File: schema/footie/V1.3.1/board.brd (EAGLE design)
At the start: 44.2 x 46.7 mm, 44 parts, among them T1 2N3565, U1 IRLML2246TRPBF, U2 USD-SOCKETNEW, U3 HC_05, U4 MCP73831, U5 3.3 regulator, U6 ATMEGA328P-AU

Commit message: finished route pcb expect antenna
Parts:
- moved C2 13.4 mm to (16.6, 41.2), turned to 0 degrees
- moved C3 7.18 mm to (30.1, 42.9), turned to 90 degrees
- moved C9 5.52 mm to (28.1, 38.9)
- moved U1 2.52 mm to (21.6, 39.2), turned to 270 degrees
- moved R9 2.11 mm to (5.48, 44.5)
- moved JP2 1.71 mm to (5.73, 36.3)
- moved U5 1.30 mm to (21.7, 43.6)
- moved C8 1.30 mm to (16.4, 43.9)
- moved U4 1.30 mm to (11.4, 42.6)
- moved C4 1.10 mm to (26.0, 43.6)
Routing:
- net +3V3: track 37.1 -> 160.4 mm, vias 1 -> 12
- net ARDUINO_TX: track 0.00 -> 81.3 mm, vias 0 -> 9
- net ARDUINO_RX: track 0.00 -> 71.4 mm, vias 0 -> 7
- net N$2: track 0.00 -> 65.1 mm, vias 0 -> 5
- net SD_MOSI: track 0.00 -> 64.7 mm, vias 0 -> 8
- net D3: track 0.00 -> 44.3 mm, vias 0 -> 2
- net D5: track 0.00 -> 43.3 mm, vias 0 -> 2
- net N$11: track 0.00 -> 43.2 mm, vias 0 -> 2
- net D2: track 0.00 -> 41.5 mm, vias 0 -> 2
- net DTR: track 0.00 -> 38.7 mm, vias 0 -> 3
- net N$20: track 0.00 -> 37.9 mm, vias 0 -> 6
- net SD_SCK: track 0.00 -> 37.3 mm, vias 0 -> 4
- net SD_MISO: track 0.00 -> 31.0 mm, vias 0 -> 1
- net GPSTX: track 0.00 -> 30.4 mm, vias 0 -> 2
- net VCC: track 0.00 -> 28.1 mm, vias 0 -> 2
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- added copper zone on layer 1, net GND
- added copper zone on layer 16, net GND
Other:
- board size 44.2 x 46.7 mm -> 46.1 x 49.1 mm

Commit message: finished route pcb expect antenna
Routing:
- net N$2: track 65.1 -> 64.0 mm
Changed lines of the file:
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@@
 <wire x1="19.2" y1="31.7" x2="21.3" y2="31.7" width="0.254" layer="16"/>
 <wire x1="18.7" y1="31.3" x2="19.2" y2="31.7" width="0.254" layer="16"/>
-<wire x1="18.7" y1="32.7" x2="18.7" y2="31.3" width="0.254" layer="1"/>
-<wire x1="11.3" y1="37" x2="18.7" y2="32.7" width="0.254" layer="1"/>
+<wire x1="17.9" y1="32.6" x2="18.7" y2="31.3" width="0.254" layer="1"/>
+<wire x1="11.3" y1="37" x2="15.5" y2="32.7" width="0.254" layer="1"/>
+<wire x1="15.5" y1="32.7" x2="16.4" y2="32.7" width="0.254" layer="1"/>
+<wire x1="16.4" y1="32.7" x2="17.9" y2="32.6" width="0.254" layer="1"/>
 <via x="13.8" y="17.8" extent="1-16" drill="0.6"/>
 <via x="20.6" y="18.1" extent="1-16" drill="0.6"/>
@@
 <wire x1="30" y1="29.6" x2="30" y2="28.5" width="0.254" layer="1"/>
 <wire x1="27.6" y1="32" x2="30" y2="29.6" width="0.254" layer="1"/>
-<wire x1="27.6" y1="34" x2="27.6" y2="32" width="0.254" layer="1"/>
-<wire x1="27.1" y1="34.5" x2="27.6" y2="34" width="0.254" layer="1"/>
-<wire x1="25.3" y1="34.5" x2="27.1" y2="34.5" width="0.254" layer="1"/>
+<wire x1="26.8" y1="33" x2="27.6" y2="32" width="0.254" layer="1"/>
+<wire x1="25.3" y1="34.5" x2="26.8" y2="33" width="0.254" layer="1"/>
 <wire x1="22.8" y1="37.2" x2="25.3" y2="34.5" width="0.254" layer="1"/>
 <wire x1="22.4" y1="36.8" x2="22.8" y2="37.2" width="0.254" layer="16"/>
@@
 <wire x1="32.5" y1="24.4" x2="32.5" y2="15.9" width="0.254" layer="16"/>
 <wire x1="28.7" y1="28.2" x2="32.5" y2="24.4" width="0.254" layer="16"/>
-<wire x1="22.8" y1="34.1" x2="28.7" y2="28.2" width="0.254" layer="1"/>
-<wire x1="22.8" y1="34.3" x2="22.8" y2="34.1" width="0.254" layer="1"/>
+<wire x1="28.4" y1="28.6" x2="28.7" y2="28.2" width="0.254" layer="1"/>
+<wire x1="22.8" y1="34.3" x2="28.4" y2="28.6" width="0.254" layer="1"/>
 <wire x1="18.4" y1="38.7" x2="22.8" y2="34.3" width="0.254" layer="1"/>
 <wire x1="15.7" y1="38.7" x2="18.4" y2="38.7" width="0.254" layer="1"/>

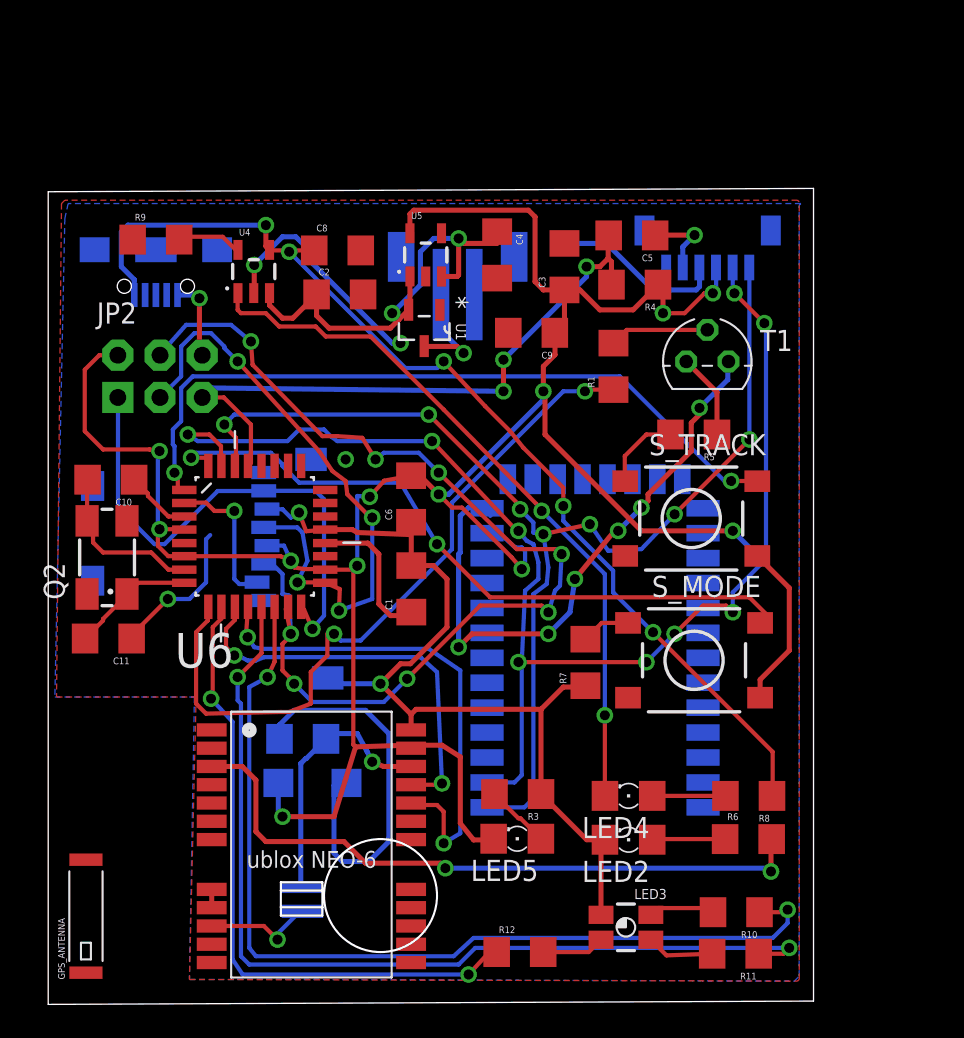
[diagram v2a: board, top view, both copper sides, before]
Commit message: complete the board layout
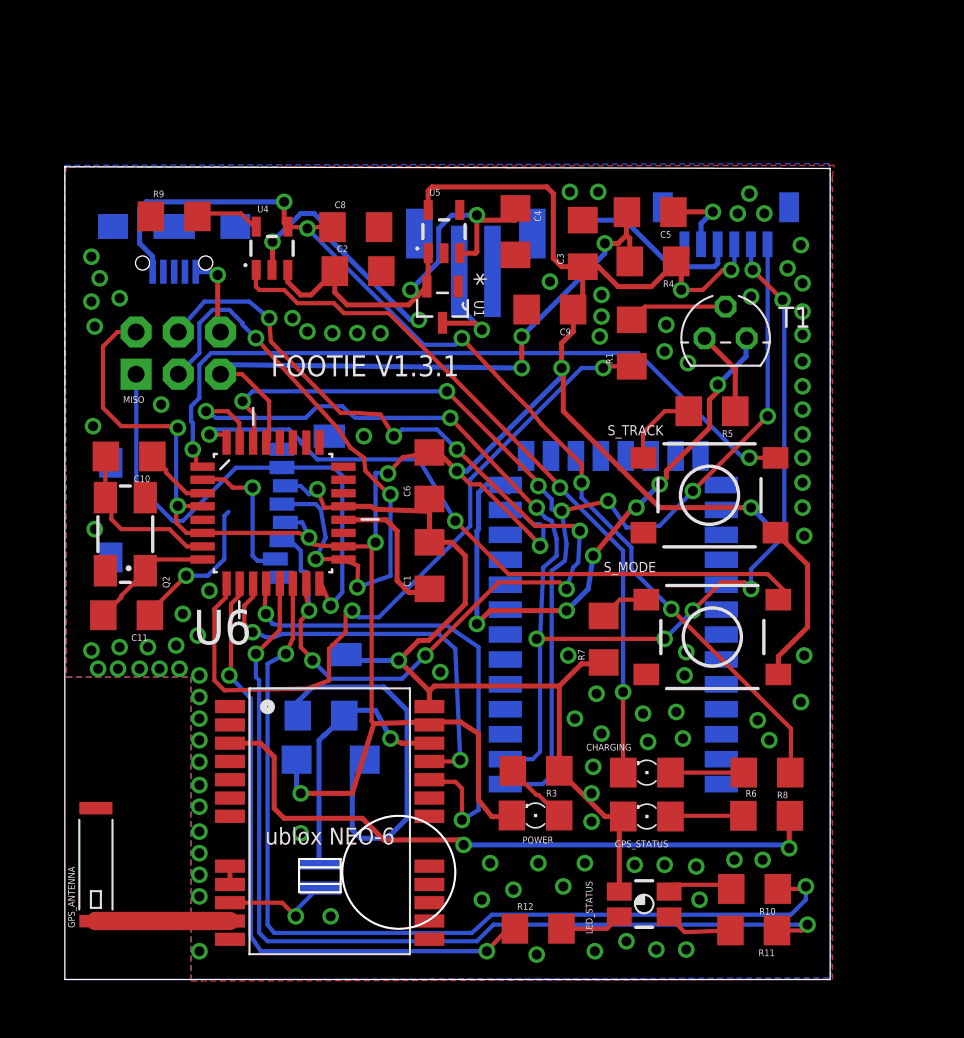
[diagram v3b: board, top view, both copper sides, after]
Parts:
- removed LED2, LED4, LED5: (no value), eagle-ltspice:LED_1206
- removed LED3: LED_RGB_PLCC_AVAGO_MTB0, pretender:LED_RGB_PLCC_AVAGO_MTB0
- removed U$2: JST_VERTICAL, SparkFun-Connectors:JST-6-SMD-VERT-1.0MM
- removed U3: HC_05, SerialPortBluetooth:BLUETOOTH_SMD
- added BLUETOOTH: HC_05, SerialPortBluetooth:BLUETOOTH_SMD
- added CHARGING, GPS_STATUS: (no value), eagle-ltspice:LED_1206
- added DEBUG: JST_VERTICAL, SparkFun-Connectors:JST-6-SMD-VERT-1.0MM
- added LED_STATUS: LED_RGB_PLCC_AVAGO_MTB0, pretender:LED_RGB_PLCC_AVAGO_MTB0
- added POWER: red, eagle-ltspice:LED_1206
- moved GPS_ANTENNA 3.16 mm to (1.87, 6.91)
- moved R5 1.78 mm to (39.0, 34.2)
- moved T1 1.78 mm to (39.8, 38.6)
- moved JP2 1.78 mm to (6.83, 37.7)
- moved C2 1.78 mm to (17.6, 42.6)
- moved R7 1.78 mm to (32.4, 20.5)
- moved C10 1.78 mm to (3.87, 31.5)
- moved C11 1.78 mm to (3.72, 21.9)
- moved Q2 1.78 mm to (3.64, 26.8)
- moved R10 1.78 mm to (41.5, 5.45)
- moved R6 1.78 mm to (42.2, 9.85)
- moved R11 1.78 mm to (41.5, 2.95)
- moved D1 1.78 mm to (16.0, 13.2)
- moved R2 1.78 mm to (15.4, 15.9)
- moved U$3 1.78 mm to (14.1, 7.25)
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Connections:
- net +3V3: now also BLUETOOTH.12, DEBUG.4, POWER.C; no longer LED5.C, U$2.4, U3.12
- net ARDUINO_RX: now also BLUETOOTH.1, DEBUG.6; no longer U$2.6, U3.1
- net ARDUINO_TX: now also BLUETOOTH.2, DEBUG.5; no longer U$2.5, U3.2
- net GND: now also BLUETOOTH.21, BLUETOOTH.22, DEBUG.3, GPS_STATUS.C, LED_STATUS.1; no longer LED2.C, LED3.1, U$2.3, U3.21, U3.22
- net N$11: now also CHARGING.C; no longer LED4.C
- net N$13: now also DEBUG.2; no longer U$2.2
- net N$16: now also POWER.A; no longer LED5.A
- net N$17: now also LED_STATUS.3; no longer LED3.3
- net N$18: now also LED_STATUS.4; no longer LED3.4
- net N$20: now also BLUETOOTH.13; no longer U3.13
- net N$21: now also LED_STATUS.2; no longer LED3.2
- net N$4: now also GPS_STATUS.A; no longer LED2.A
- net N$8: now also CHARGING.A; no longer LED4.A
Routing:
- net N$7: track 0.00 -> 8.08 mm
- net GND: vias 8 -> 108
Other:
- board size 46.1 x 49.1 mm -> 46.1 x 48.9 mm
- board text added: "FOOTIE V1.3.1"
- board text added: "MISO"

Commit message: complete board but not happy
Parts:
- removed GPS_ANTENNA: ANTENNA2SMD6, SparkFun-RF:ANTENNA-CHIP6
- removed U$1: UBLOX_NEO-6, Ava:UBLOX_NEO-6P
- added C7: 4.7 uF, SparkFun-Capacitors:1206
- added R13, R14: 220 Ohm, SparkFun-Passives:1206
- added U3: CAM-M8Q, CAM-M8Q:CAM-M8Q
- moved BLUETOOTH 38.1 mm to (40.7, 47.1), turned to 0 degrees
- moved R5 32.7 mm to (24.1, 5.08), flipped to the bottom, turned to 0 degrees
- moved S_TRACK 28.2 mm to (24.1, 5.08)
- moved BATTERY_CONNECTOR 21.9 mm to (4.28, 52.5), flipped to the top
- moved C3 20.7 mm to (10.5, 43.7), turned to 0 degrees
- moved R6 19.5 mm to (23.5, 15.1), turned to 180 degrees
- moved R8 18.8 mm to (23.5, 12.5), turned to 0 degrees
- moved C4 18.4 mm to (10.6, 53.2)
- moved R9 17.2 mm to (23.8, 46.0), turned to 90 degrees
- moved T1 16.4 mm to (37.5, 22.3)
- moved U2 16.3 mm to (16.3, 41.6), turned to 270 degrees
- moved U1 16.1 mm to (8.19, 47.4), turned to 90 degrees
- moved R7 16.0 mm to (36.8, 5.08), flipped to the bottom, turned to 0 degrees
- moved S_MODE 15.7 mm to (36.8, 5.08)
- moved R1 15.6 mm to (32.6, 22.8)
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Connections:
- removed net N$6 (its old number): R2.1, U$1.22_V_BCKP, U$3.3V
- removed net N$7: GPS_ANTENNA.1, U$1.11_RF_IN
- removed net SCL: U$1.19_SCL2
- removed net SDA: U$1.18_SDA2
- new net N$25: R13.1, U3.25
- new net N$26: R14.1, U3.26
- new net N$4: R6.2, U3.29
- net +3V3: now also C7.1, U3.1, U3.9; no longer U$1.23_VCC
- net GND: now also C7.2, U3.10, U3.11, U3.12, U3.13, U3.14, U3.15, U3.18, U3.19, U3.21, U3.22, U3.27, U3.31, U3.4, U3.5; no longer U$1.10_GND, U$1.12_GND, U$1.13_GND, U$1.24_GND, U$1.7_VDDUSB
- net GPSRX: now also R14.2; no longer U$1.21_RXD1
- net GPSTX: now also R13.2; no longer U$1.20_TXD1
- net N$3: now also U3.16, U3.17; no longer R6.2, U$1.3_TIMEPULSE
- net N$5: now also R2.1, U$3.3V, U3.8; no longer U$1.8_RESERVED, U$1.9_VCC_RF
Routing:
- net GND: track 111.9 -> 280.7 mm, vias 108 -> 71
- net +3V3: track 160.4 -> 245.0 mm, vias 12 -> 16
- net N$3: track 40.1 -> 1.00 mm, vias 2 -> 0
- net ARDUINO_TX: track 81.3 -> 43.3 mm, vias 9 -> 3
- net D10: track 57.3 -> 22.0 mm
- net N$5: track 1.10 -> 35.1 mm, vias 0 -> 2
- net N$20: track 37.9 -> 7.60 mm, vias 6 -> 0
- net D9: track 57.3 -> 27.7 mm, vias 2 -> 0
- net ARDUINO_RX: track 71.4 -> 44.3 mm, vias 7 -> 4
- net GPSTX: track 30.4 -> 7.66 mm, vias 2 -> 0
- net N$1: track 23.8 -> 2.10 mm
- net N$2: track 64.0 -> 84.9 mm, vias 5 -> 6
- net DTR: track 38.7 -> 58.4 mm, vias 3 -> 7
- net SD_CS: track 8.87 -> 26.8 mm
- net D5: track 43.3 -> 25.5 mm, vias 2 -> 4
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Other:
- board size 46.1 x 48.9 mm -> 42.9 x 57 mm
- board text removed: "FOOTIE V1.3.1"
- board text removed: "MISO"

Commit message: update version, bit bigger but better design
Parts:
- moved BATTERY_CONNECTOR 48.5 mm to (48.4, 32.1), turned to 270 degrees
- moved U1 39.5 mm to (42.7, 28.3), turned to 270 degrees
- moved C4 33.9 mm to (39.7, 35.8), turned to 180 degrees
- moved C3 32.0 mm to (38.3, 27.9), turned to 270 degrees
- moved U5 31.2 mm to (39.8, 32.2)
- moved C9 26.2 mm to (35.5, 27.8)
- moved C5 20.7 mm to (43.7, 42.3), turned to 270 degrees
- moved R11 15.2 mm to (48.5, 6.81), turned to 180 degrees
- moved R10 15.0 mm to (43.8, 3.90), turned to 270 degrees
- moved R1 14.3 mm to (43.2, 13.2)
- moved R12 14.1 mm to (48.5, 9.58)
- moved LED_STATUS 12.5 mm to (48.5, 2.84), turned to 270 degrees
- moved JP2 12.2 mm to (19.9, 41.5), turned to 90 degrees
- moved C8 12.1 mm to (32.1, 40.3), turned to 270 degrees
- moved BLUETOOTH 11.2 mm to (48.9, 39.5)
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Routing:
- net GND: track 280.7 -> 203.3 mm, vias 71 -> 56
- net +3V3: track 245.0 -> 187.5 mm, vias 16 -> 14
- net N$2: track 84.9 -> 39.1 mm, vias 6 -> 2
- net SD_MOSI: track 71.7 -> 35.7 mm, vias 7 -> 6
- net N$11: track 52.2 -> 29.2 mm, vias 4 -> 2
- net ARDUINO_TX: track 43.3 -> 62.0 mm
- net D9: track 27.7 -> 45.8 mm, vias 0 -> 2
- net DTR: track 58.4 -> 41.2 mm, vias 7 -> 3
- net D10: track 22.0 -> 37.0 mm
- net D6: track 34.0 -> 48.8 mm
- net D5: track 25.5 -> 39.1 mm, vias 4 -> 2
- net SD_MISO: track 29.8 -> 42.0 mm, vias 2 -> 4
- net SD_CS: track 26.8 -> 16.6 mm
- net N$13: track 10.5 -> 2.30 mm, vias 2 -> 0
- net ARDUINO_RX: track 44.3 -> 51.3 mm, vias 4 -> 5
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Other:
- board size 42.9 x 57 mm -> 53 x 50.6 mm

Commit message: update final version + library
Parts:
- S_MODE: value DTSM-6 -> MODE
- S_TRACK: value DTSM-6 -> TRACK
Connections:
- net GND: no longer BLUETOOTH.21, BLUETOOTH.22
- net N$20: now also BLUETOOTH.21, BLUETOOTH.22
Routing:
- net N$20: track 13.8 -> 28.7 mm
- net ARDUINO_TX: track 62.0 -> 63.1 mm
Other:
- board text added: "FOOTIE V1.3.1"

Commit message: update stuff2
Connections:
- net +3V3: now also LED_STATUS.1
- net GND: no longer LED_STATUS.1
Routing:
- net GND: track 203.3 -> 188.5 mm, vias 56 -> 54
- net +3V3: track 187.5 -> 198.0 mm, vias 14 -> 16
- net N$2: track 39.1 -> 41.8 mm
- net DTR: track 41.2 -> 43.0 mm
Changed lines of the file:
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@@
 </element>
 <element name="C7" library="SparkFun-Capacitors" package="1206" value="4.7 uF" x="3.2" y="17.04">
-<attribute name="OC_FARNELL" value="2497081" x="3.2" y="17.04" size="1.778" layer="27" display="off"/>
+<attribute name="OC_FARNELL" value="2497114" x="3.2" y="17.04" size="1.778" layer="27" display="off"/>
 <attribute name="MF" value="WALSIN" x="3.2" y="17.04" size="1.778" layer="27" display="off"/>
-<attribute name="MPN" value="1206B106K160CT" x="3.2" y="17.04" size="1.778" layer="27" display="off"/>
+<attribute name="MPN" value="1206B475K500CT" x="3.2" y="17.04" size="1.778" layer="27" display="off"/>
 </element>
 <element name="C8" library="SparkFun-Capacitors" package="1206" value="4.7 uF" x="32.07" y="40.26" rot="R270">
@@
 <attribute name="VALUE" x="10.43" y="44.11" size="0.8128" layer="28" rot="MR270" display="off"/>
 </element>
-<element name="U3" library="CAM-M8Q" package="CAM-M8Q" value="CAM-M8Q" x="9.29" y="7.82" rot="R180"/>
+<element name="U3" library="CAM-M8Q" package="CAM-M8Q" value="CAM-M8Q" x="9.29" y="7.82" rot="R180">
+<attribute name="OC_FARNELL" value="unknown" x="9.29" y="7.82" size="1.778" layer="27" rot="R180" display="off"/>
+<attribute name="MF" value="" x="9.29" y="7.82" size="1.778" layer="27" rot="R180" display="off"/>
+<attribute name="MPN" value="" x="9.29" y="7.82" size="1.778" layer="27" rot="R180" display="off"/>
+</element>
 <element name="U4" library="SparkFun-PowerIC" package="SOT23-5" value="MCP73831" x="28.51" y="40.26">
 <attribute name="OC_FARNELL" value="1332158" x="28.51" y="40.26" size="1.778" layer="27" display="off"/>
@@
 <wire x1="18.7" y1="38.9" x2="18.64" y2="38.93" width="0.254" layer="1"/>
 <wire x1="23.5" y1="35.3" x2="23.55" y2="36.11" width="0.254" layer="1"/>
+<contactref element="LED_STATUS" pad="1"/>
+<wire x1="41.6" y1="2.5" x2="40.9" y2="2.5" width="0.254" layer="1"/>
+<wire x1="43" y1="3.9" x2="41.6" y2="2.5" width="0.254" layer="1"/>
+<wire x1="45.5" y1="3.9" x2="43" y2="3.9" width="0.254" layer="1"/>
+<wire x1="47.4" y1="3.9" x2="45.5" y2="3.9" width="0.254" layer="16"/>
+<wire x1="48.5" y1="2.8" x2="47.4" y2="3.9" width="0.254" layer="16"/>
+<wire x1="49.2" y1="2.1" x2="48.5" y2="2.8" width="0.254" layer="1"/>
+<wire x1="50" y1="2.1" x2="49.2" y2="2.1" width="0.254" layer="1"/>
+<wire x1="40.9" y1="2.5" x2="40.805" y2="2.53" width="0.254" layer="1"/>
+<wire x1="50" y1="2.1" x2="50.05" y2="2.09" width="0.254" layer="1"/>
+<via x="45.5" y="3.9" extent="1-16" drill="0.6"/>
+<via x="48.5" y="2.8" extent="1-16" drill="0.6"/>
 </signal>
 <signal name="GPSRX">
@@
 <wire x1="39.4" y1="42.4" x2="26.1" y2="42.4" width="0.254" layer="16"/>
 <wire x1="41.6" y1="42.4" x2="39.4" y2="42.4" width="0.254" layer="1"/>
-<wire x1="43.1" y1="40.9" x2="41.6" y2="42.4" width="0.254" layer="1"/>
+<wire x1="43.1" y1="40.9" x2="42.75" y2="41.25" width="0.254" layer="1"/>
+<wire x1="42.75" y1="41.25" x2="41.6" y2="42.4" width="0.254" layer="1"/>
 <wire x1="43.7" y1="40.9" x2="43.1" y2="40.9" width="0.254" layer="1"/>
 <wire x1="21.2" y1="44" x2="21.18" y2="44.01" width="0.254" layer="1"/>
@@
 <via x="23.2" y="44" extent="1-16" drill="0.6"/>
 <via x="39.4" y="42.4" extent="1-16" drill="0.6"/>
-<wire x1="41.6" y1="42.4" x2="41.06" y2="40.79" width="0" layer="19" extent="1-1"/>
+<wire x1="42.3" y1="40.8" x2="42.75" y2="41.25" width="0.254" layer="1"/>
+<wire x1="41.1" y1="40.8" x2="42.3" y2="40.8" width="0.254" layer="1"/>
+<wire x1="41.1" y1="40.8" x2="41.06" y2="40.79" width="0.254" layer="1"/>
 </signal>
 <signal name="N$2">
@@
 <via x="28.9" y="40.3" extent="1-16" drill="0.6"/>
 <via x="28.9" y="20.1" extent="1-16" drill="0.6"/>
-<wire x1="29.5" y1="41.5" x2="32.07" y2="41.66" width="0" layer="19" extent="1-1"/>
+<wire x1="30.5" y1="41.5" x2="29.6" y2="41.5" width="0.254" layer="1"/>
+<wire x1="30.7" y1="41.7" x2="30.5" y2="41.5" width="0.254" layer="1"/>
+<wire x1="32" y1="41.7" x2="30.7" y2="41.7" width="0.254" layer="1"/>
+<wire x1="29.6" y1="41.5" x2="29.46" y2="41.5601" width="0.254" layer="1"/>
+<wire x1="32" y1="41.7" x2="32.07" y2="41.66" width="0.254" layer="1"/>
 </signal>
 <signal name="N$11">
@@
 <contactref element="BATTERY_CONNECTOR" pad="VCC"/>
 <contactref element="U1" pad="1"/>
-<contactref element="LED_STATUS" pad="1"/>
 <contactref element="U3" pad="14"/>
 <contactref element="U3" pad="15"/>
@@
 <via x="39.8" y="27.8" extent="1-16" drill="0.6"/>
 <via x="39.8" y="30.7" extent="1-16" drill="0.6"/>
-<wire x1="39.6" y1="5.1" x2="38.2" y2="5.1" width="0.254" layer="1"/>
-<wire x1="39.8" y1="4.9" x2="39.6" y2="5.1" width="0.254" layer="1"/>
-<wire x1="41" y1="6.1" x2="39.8" y2="4.9" width="0.254" layer="16"/>
-<wire x1="45.6" y1="6.1" x2="41" y2="6.1" width="0.254" layer="16"/>
-<wire x1="48.6" y1="2.8" x2="45.6" y2="6.1" width="0.254" layer="16"/>
-<wire x1="49.6" y1="2.1" x2="48.6" y2="2.8" width="0.254" layer="1"/>
-<wire x1="50.4" y1="2.1" x2="49.6" y2="2.1" width="0.254" layer="1"/>
-<wire x1="50.4" y1="2.1" x2="50.05" y2="2.09" width="0.254" layer="1"/>
-<via x="39.8" y="4.9" extent="1-16" drill="0.6"/>
-<via x="48.6" y="2.8" extent="1-16" drill="0.6"/>
 </signal>
 <signal name="N$10">
